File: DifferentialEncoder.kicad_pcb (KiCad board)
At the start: 2 copper layers, 17.8 x 12.7 mm, 8 parts, among them J1 Conn_02x04_Odd_Even, J2 ODrive Connector, U1 MAX3284E, U2 MAX3284E, U3 MAX3284E

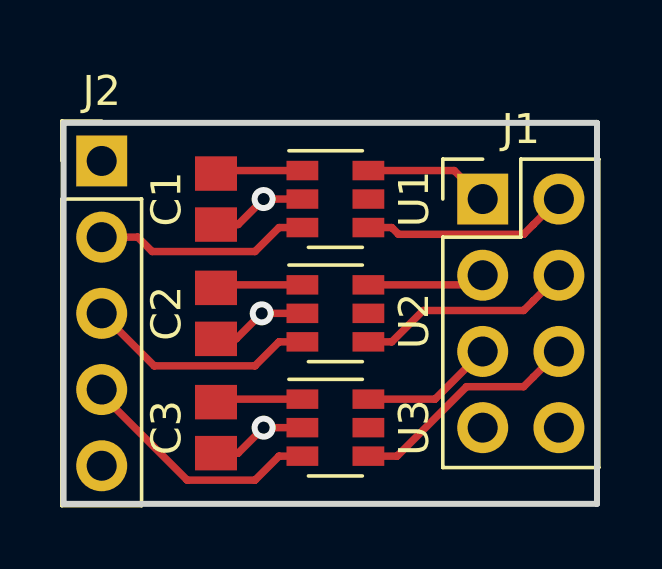
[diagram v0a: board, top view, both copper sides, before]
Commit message: Change some silkscreen, flip single-ended pins to back side
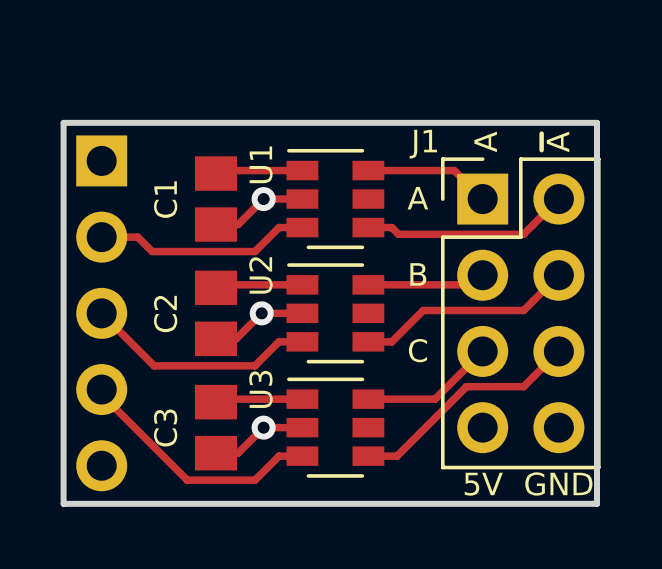
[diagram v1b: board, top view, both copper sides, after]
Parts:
- J2: moved to B.Cu
- turned J2 to 180 degrees
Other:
- board text added: "5V"
- board text added: "5v"
- board text added: "A"
- board text added: "B"
- board text added: "C"
- board text added: "Differential Encoder Adapter Wetmelon 2018-08-19"
- board text added: "GND"
- board text added: "~A"
- board text removed: "Differential Encoder Adapter Wetmelon 2018-08-15"
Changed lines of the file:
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@@
   (general
     (thickness 1.6)
-    (drawings 5)
+    (drawings 14)
     (tracks 53)
     (zones 0)
@@
     (pad_to_mask_clearance 0.2)
     (aux_axis_origin 0 0)
-    (visible_elements FFFFFF7F)
+    (visible_elements 7FFFFFFF)
     (pcbplotparams
       (layerselection 0x010fc_ffffffff)
@@
     (attr smd)
     (fp_text reference C1 (at 0 1.651 270) (layer F.SilkS)
-      (effects (font (size 1 1) (thickness 0.15)))
+      (effects (font (size 0.75 0.75) (thickness 0.15)))
     )
     (fp_text value 100nF (at 0 1.65 270) (layer F.Fab)
@@
     (attr smd)
     (fp_text reference C2 (at 0 1.651 270) (layer F.SilkS)
-      (effects (font (size 1 1) (thickness 0.15)))
+      (effects (font (size 0.75 0.75) (thickness 0.15)))
     )
     (fp_text value 100nF (at 0 1.65 270) (layer F.Fab)
@@
     (attr smd)
     (fp_text reference C3 (at 0 1.651 270) (layer F.SilkS)
-      (effects (font (size 1 1) (thickness 0.15)))
+      (effects (font (size 0.75 0.75) (thickness 0.15)))
     )
     (fp_text value 100nF (at 0 1.65 270) (layer F.Fab)
@@
     (descr "Through hole straight pin header, 2x04, 2.54mm pitch, double rows")
     (tags "Through hole pin header THT 2x04 2.54mm double row")
-    (fp_text reference J1 (at 1.27 -2.33) (layer F.SilkS)
-      (effects (font (size 1 1) (thickness 0.15)))
+    (fp_text reference J1 (at -1.905 -1.905 180) (layer F.SilkS)
+      (effects (font (size 0.75 0.75) (thickness 0.15)))
     )
     (fp_text value Conn_02x04_Odd_Even (at 1.27 9.95) (layer F.Fab)
@@
     )
   )
-  (module Connector_PinHeader_2.54mm:PinHeader_1x05_P2.54mm_Vertical (layer F.Cu)
-    (at 181.61 74.93)
+  (module Connector_PinHeader_2.54mm:PinHeader_1x05_P2.54mm_Vertical (layer B.Cu)
+    (at 181.61 74.93 180)
     (descr "Through hole straight pin header, 1x05, 2.54mm pitch, single row")
     (tags "Through hole pin header THT 1x05 2.54mm single row")
-    (fp_text reference J2 (at 0 -2.33) (layer F.SilkS)
-      (effects (font (size 1 1) (thickness 0.15)))
-    )
-    (fp_text value "ODrive Connector" (at 0 12.49) (layer F.Fab)
-      (effects (font (size 1 1) (thickness 0.15)))
-    )
-    (fp_line (start -0.635 -1.27) (end 1.27 -1.27) (layer F.Fab) (width 0.1))
-    (fp_line (start 1.27 -1.27) (end 1.27 11.43) (layer F.Fab) (width 0.1))
-    (fp_line (start 1.27 11.43) (end -1.27 11.43) (layer F.Fab) (width 0.1))
-    (fp_line (start -1.27 11.43) (end -1.27 -0.635) (layer F.Fab) (width 0.1))
-    (fp_line (start -1.27 -0.635) (end -0.635 -1.27) (layer F.Fab) (width 0.1))
-    (fp_line (start -1.33 11.49) (end 1.33 11.49) (layer F.SilkS) (width 0.12))
-    (fp_line (start -1.33 1.27) (end -1.33 11.49) (layer F.SilkS) (width 0.12))
-    (fp_line (start 1.33 1.27) (end 1.33 11.49) (layer F.SilkS) (width 0.12))
-    (fp_line (start -1.33 1.27) (end 1.33 1.27) (layer F.SilkS) (width 0.12))
-    (fp_line (start -1.33 0) (end -1.33 -1.33) (layer F.SilkS) (width 0.12))
-    (fp_line (start -1.33 -1.33) (end 0 -1.33) (layer F.SilkS) (width 0.12))
-    (fp_line (start -1.8 -1.8) (end -1.8 11.95) (layer F.CrtYd) (width 0.05))
-    (fp_line (start -1.8 11.95) (end 1.8 11.95) (layer F.CrtYd) (width 0.05))
-    (fp_line (start 1.8 11.95) (end 1.8 -1.8) (layer F.CrtYd) (width 0.05))
-    (fp_line (start 1.8 -1.8) (end -1.8 -1.8) (layer F.CrtYd) (width 0.05))
-    (fp_text user %R (at 0 5.08 90) (layer F.Fab)
-      (effects (font (size 1 1) (thickness 0.15)))
-    )
-    (pad 1 thru_hole rect (at 0 0) (size 1.7 1.7) (drill 1) (layers *.Cu *.Mask)
-      (net 2 +5V))
-    (pad 2 thru_hole oval (at 0 2.54) (size 1.7 1.7) (drill 1) (layers *.Cu *.Mask)
+    (fp_text reference J2 (at 0 2.33 180) (layer B.SilkS)
+      (effects (font (size 1 1) (thickness 0.15)) (justify mirror))
+    )
+    (fp_text value "ODrive Connector" (at 0 -12.49 180) (layer B.Fab)
+      (effects (font (size 1 1) (thickness 0.15)) (justify mirror))
+    )
+    (fp_line (start -0.635 1.27) (end 1.27 1.27) (layer B.Fab) (width 0.1))
+    (fp_line (start 1.27 1.27) (end 1.27 -11.43) (layer B.Fab) (width 0.1))
+    (fp_line (start 1.27 -11.43) (end -1.27 -11.43) (layer B.Fab) (width 0.1))
+    (fp_line (start -1.27 -11.43) (end -1.27 0.635) (layer B.Fab) (width 0.1))
+    (fp_line (start -1.27 0.635) (end -0.635 1.27) (layer B.Fab) (width 0.1))
+    (fp_line (start -1.33 -11.49) (end 1.33 -11.49) (layer B.SilkS) (width 0.12))
+    (fp_line (start -1.33 -1.27) (end -1.33 -11.49) (layer B.SilkS) (width 0.12))
+    (fp_line (start 1.33 -1.27) (end 1.33 -11.49) (layer B.SilkS) (width 0.12))
+    (fp_line (start -1.33 -1.27) (end 1.33 -1.27) (layer B.SilkS) (width 0.12))
+    (fp_line (start -1.33 0) (end -1.33 1.33) (layer B.SilkS) (width 0.12))
+    (fp_line (start -1.33 1.33) (end 0 1.33) (layer B.SilkS) (width 0.12))
+    (fp_line (start -1.8 1.8) (end -1.8 -11.95) (layer B.CrtYd) (width 0.05))
+    (fp_line (start -1.8 -11.95) (end 1.8 -11.95) (layer B.CrtYd) (width 0.05))
+    (fp_line (start 1.8 -11.95) (end 1.8 1.8) (layer B.CrtYd) (width 0.05))
+    (fp_line (start 1.8 1.8) (end -1.8 1.8) (layer B.CrtYd) (width 0.05))
+    (fp_text user %R (at 0 -5.08 90) (layer B.Fab)
+      (effects (font (size 1 1) (thickness 0.15)) (justify mirror))
+    )
+    (pad 1 thru_hole rect (at 0 0 180) (size 1.7 1.7) (drill 1) (layers *.Cu *.Mask)
+      (net 2 +5V))
+    (pad 2 thru_hole oval (at 0 -2.54 180) (size 1.7 1.7) (drill 1) (layers *.Cu *.Mask)
       (net 9 /A_Out))
-    (pad 3 thru_hole oval (at 0 5.08) (size 1.7 1.7) (drill 1) (layers *.Cu *.Mask)
+    (pad 3 thru_hole oval (at 0 -5.08 180) (size 1.7 1.7) (drill 1) (layers *.Cu *.Mask)
       (net 10 /B_Out))
-    (pad 4 thru_hole oval (at 0 7.62) (size 1.7 1.7) (drill 1) (layers *.Cu *.Mask)
+    (pad 4 thru_hole oval (at 0 -7.62 180) (size 1.7 1.7) (drill 1) (layers *.Cu *.Mask)
       (net 11 /Z_Out))
-    (pad 5 thru_hole oval (at 0 10.16) (size 1.7 1.7) (drill 1) (layers *.Cu *.Mask)
+    (pad 5 thru_hole oval (at 0 -10.16 180) (size 1.7 1.7) (drill 1) (layers *.Cu *.Mask)
       (net 1 GND))
     (model ${KISYS3DMOD}/Connector_PinHeader_2.54mm.3dshapes/PinHeader_1x05_P2.54mm_Vertical.wrl
@@
     (tags SOT-23-6)
     (attr smd)
-    (fp_text reference U1 (at 2.624 0 90) (layer F.SilkS)
-      (effects (font (size 1 1) (thickness 0.15)))
+    (fp_text reference U1 (at -2.456 -1.143 90) (layer F.SilkS)
+      (effects (font (size 0.75 0.75) (thickness 0.15)))
     )
     (fp_text value MAX3284E (at 0 2.9) (layer F.Fab)
@@
     (tags SOT-23-6)
     (attr smd)
-    (fp_text reference U2 (at 2.624 0.254 90) (layer F.SilkS)
-      (effects (font (size 1 1) (thickness 0.15)))
+    (fp_text reference U2 (at -2.456 -1.27 90) (layer F.SilkS)
+      (effects (font (size 0.75 0.75) (thickness 0.15)))
     )
     (fp_text value MAX3284E (at 0 2.9) (layer F.Fab)
@@
     (tags SOT-23-6)
     (attr smd)
-    (fp_text reference U3 (at 2.624 0 90) (layer F.SilkS)
-      (effects (font (size 1 1) (thickness 0.15)))
+    (fp_text reference U3 (at -2.456 -1.27 90) (layer F.SilkS)
+      (effects (font (size 0.75 0.75) (thickness 0.15)))
     )
     (fp_text value MAX3284E (at 0 2.9) (layer F.Fab)
@@
     )
   )
-  (gr_text "Differential\nEncoder Adapter\n\nWetmelon\n2018-08-15" (at 192.786 78.105) (layer B.SilkS)
+  (gr_text GND (at 196.85 85.725) (layer F.SilkS)
+    (effects (font (size 0.75 0.75) (thickness 0.15)))
+  )
+  (gr_text 5V (at 194.31 85.725) (layer F.SilkS)
+    (effects (font (size 0.75 0.75) (thickness 0.15)))
+  )
+  (gr_text C (at 192.151 81.28) (layer F.SilkS)
+    (effects (font (size 0.75 0.75) (thickness 0.15)))
+  )
+  (gr_text B (at 192.151 78.74) (layer F.SilkS)
+    (effects (font (size 0.75 0.75) (thickness 0.15)))
+  )
+  (gr_text A (at 192.151 76.2) (layer F.SilkS)
+    (effects (font (size 0.75 0.75) (thickness 0.15)))
+  )
+  (gr_text ~A (at 196.85 74.295 90) (layer F.SilkS)
+    (effects (font (size 0.75 0.75) (thickness 0.15)))
+  )
+  (gr_text A (at 194.437 74.295 90) (layer F.SilkS)
+    (effects (font (size 0.75 0.75) (thickness 0.15)))
+  )
+  (gr_text GND (at 184.658 85.217) (layer B.SilkS)
+    (effects (font (size 0.75 0.75) (thickness 0.15)) (justify mirror))
+  )
+  (gr_text 5v (at 184.277 74.93) (layer B.SilkS)
+    (effects (font (size 0.75 0.75) (thickness 0.15)) (justify mirror))
+  )
+  (gr_text "Differential\nEncoder Adapter\n\nWetmelon\n2018-08-19" (at 192.786 80.01) (layer B.SilkS)
     (effects (font (size 0.75 0.75) (thickness 0.1)) (justify left mirror))
   )

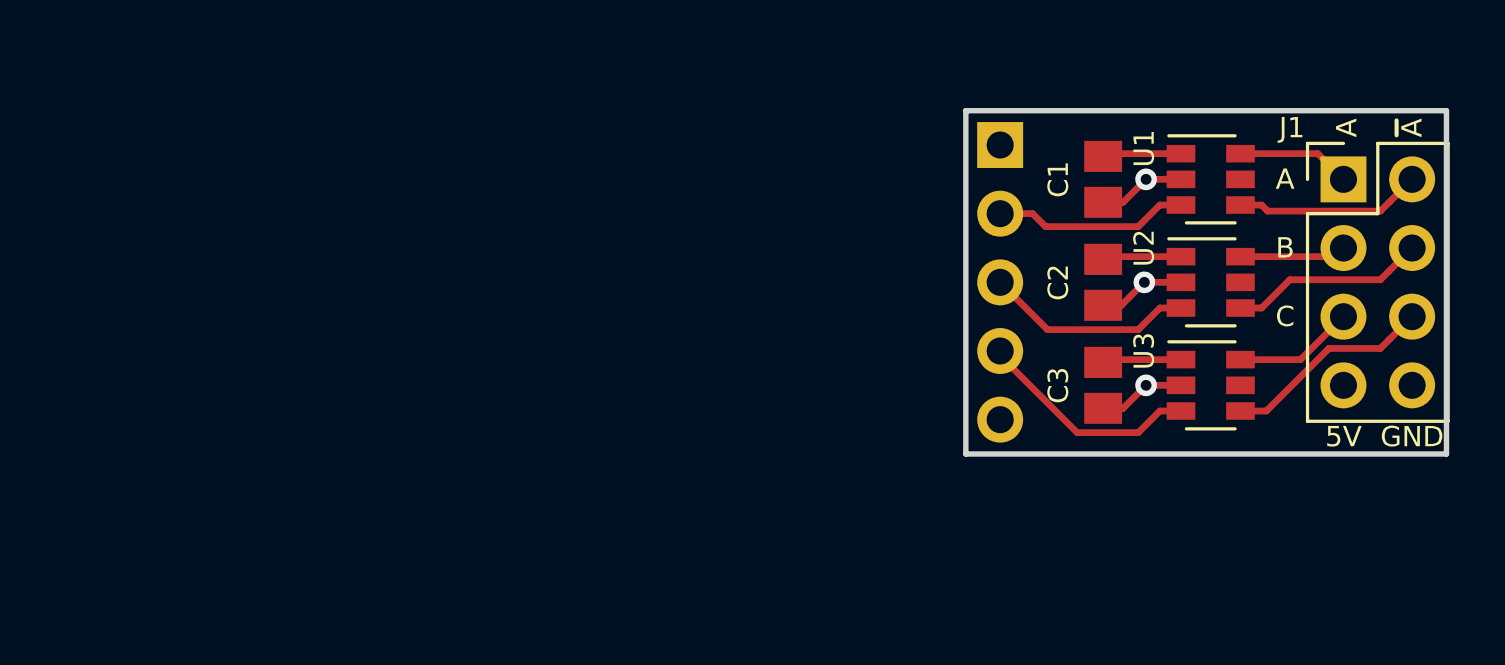
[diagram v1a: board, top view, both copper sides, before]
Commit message: Update differential adapter with termination etc.
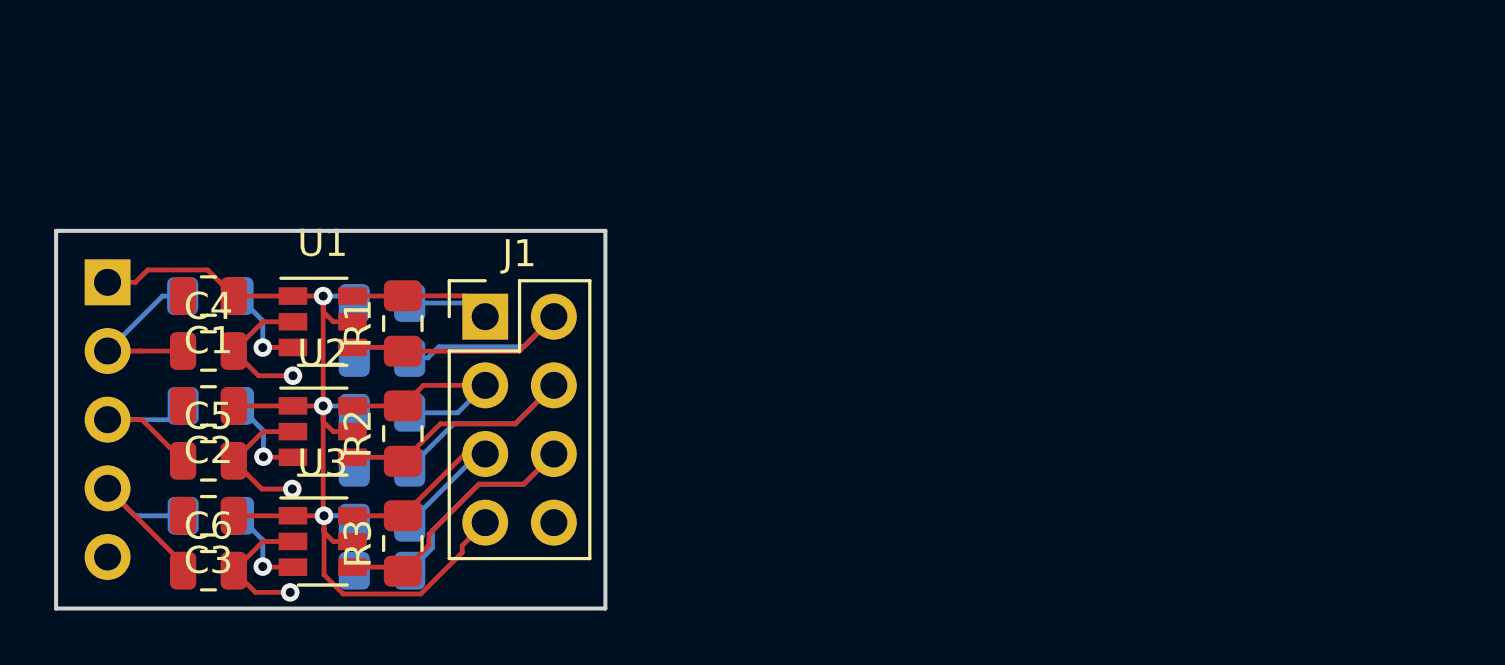
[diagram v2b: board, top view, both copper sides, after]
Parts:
- added C4: 1nF, Capacitor_SMD:C_0805_2012Metric, F.Cu at (152.3, 82.5)
- added C5: 1nF, Capacitor_SMD:C_0805_2012Metric, F.Cu at (152.3, 86.6)
- added C6: 1nF, Capacitor_SMD:C_0805_2012Metric, F.Cu at (152.3, 90.7)
- added R1: 120, Resistor_SMD:R_0805_2012Metric_Pad1.15x1.40mm_HandSolder, F.Cu at (159.5, 81.5)
- added R10: 2K, Resistor_SMD:R_0805_2012Metric_Pad1.15x1.40mm_HandSolder, B.Cu at (158.7, 80.8)
- added R11: 2K, Resistor_SMD:R_0805_2012Metric_Pad1.15x1.40mm_HandSolder, B.Cu at (158.7, 82.8)
- added R12: 2K, Resistor_SMD:R_0805_2012Metric_Pad1.15x1.40mm_HandSolder, B.Cu at (158.7, 84.8)
- added R13: 2K, Resistor_SMD:R_0805_2012Metric_Pad1.15x1.40mm_HandSolder, B.Cu at (158.7, 86.9)
- added R14: 2K, Resistor_SMD:R_0805_2012Metric_Pad1.15x1.40mm_HandSolder, B.Cu at (158.7, 88.9)
- added R15: 2K, Resistor_SMD:R_0805_2012Metric_Pad1.15x1.40mm_HandSolder, B.Cu at (158.7, 90.7)
- added R2: 120, Resistor_SMD:R_0805_2012Metric_Pad1.15x1.40mm_HandSolder, F.Cu at (159.5, 85.6)
- added R3: 120, Resistor_SMD:R_0805_2012Metric_Pad1.15x1.40mm_HandSolder, F.Cu at (159.5, 89.7)
- added R4: 10, Resistor_SMD:R_0805_2012Metric_Pad1.15x1.40mm_HandSolder, B.Cu at (152.4, 80.5)
- added R5: 10, Resistor_SMD:R_0805_2012Metric_Pad1.15x1.40mm_HandSolder, B.Cu at (152.4, 84.6)
- added R6: 10, Resistor_SMD:R_0805_2012Metric_Pad1.15x1.40mm_HandSolder, B.Cu at (152.4, 88.6)
- moved C3 33.4 mm to (152.3, 88.6), turned to 180 degrees
- moved C2 33.4 mm to (152.3, 84.6), turned to 180 degrees
- moved J2 33.4 mm to (148.6, 80.0)
- moved C1 33.4 mm to (152.3, 80.5), turned to 180 degrees
- moved U3 33.4 mm to (156.5, 89.6)
- moved U2 33.3 mm to (156.5, 85.5)
- moved U1 33.3 mm to (156.5, 81.5)
- moved J1 32.2 mm to (162.6, 81.3)
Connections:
- U1 pad 3: /A_Out -> Net-(R4-Pad1)
- U2 pad 3: /B_Out -> Net-(R5-Pad1)
- U3 pad 3: /Z_Out -> Net-(R6-Pad1)
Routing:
- net +5V: track 8.76 -> 41.7 mm, vias 0 -> 3
- net /~Z: track 7.80 -> 17.0 mm
- net /~B: track 7.27 -> 15.3 mm
- net /~A: track 6.93 -> 14.0 mm
- net GND: track 9.70 -> 15.5 mm
- net /Z: track 4.47 -> 9.70 mm
- net /B: track 3.94 -> 8.44 mm
- net /A: track 4.20 -> 8.24 mm
- net Net-(R4-Pad1): track 0.00 -> 3.40 mm, vias 0 -> 1
- net Net-(R6-Pad1): track 0.00 -> 3.38 mm, vias 0 -> 1
- net Net-(R5-Pad1): track 0.00 -> 3.36 mm, vias 0 -> 1
- net /B_Out: track 7.75 -> 6.43 mm
- net /Z_Out: track 8.37 -> 7.42 mm
- net /A_Out: track 7.22 -> 6.41 mm
- added copper zone on F.Cu, net GND
- removed copper zone on F.Cu, net +5V
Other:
- board size 17.8 x 12.7 mm -> 20.3 x 14 mm
- net class Default: clearance 0.2 -> 0.1778; trace_width 0.25 -> 0.1778; via_dia 0.8 -> 0.6858; via_drill 0.4 -> 0.3302
- rule pad_to_mask_clearance: 0.2 -> 0.0508
- rule trace_clearance: 0.2 -> 0.1778
- rule trace_min: 0.2 -> 0.1778
- rule via_min_drill: 0.3 -> 0.3302
- rule via_min_size: 0.4 -> 0.6858
- board text added: "ODrive Side"
- board text removed: "5V"
- board text removed: "5v"
- board text removed: "A"
- board text removed: "B"
- board text removed: "C"
- board text removed: "Differential Encoder Adapter Wetmelon 2018-08-19"
- board text removed: "GND"
- board text removed: "~A"
